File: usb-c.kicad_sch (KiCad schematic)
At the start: 16 parts, among them IC1 USBLC6-2SC6, IC2 632723100011, IC3 TCPP01-M12, Q1 STL11N3LLH6

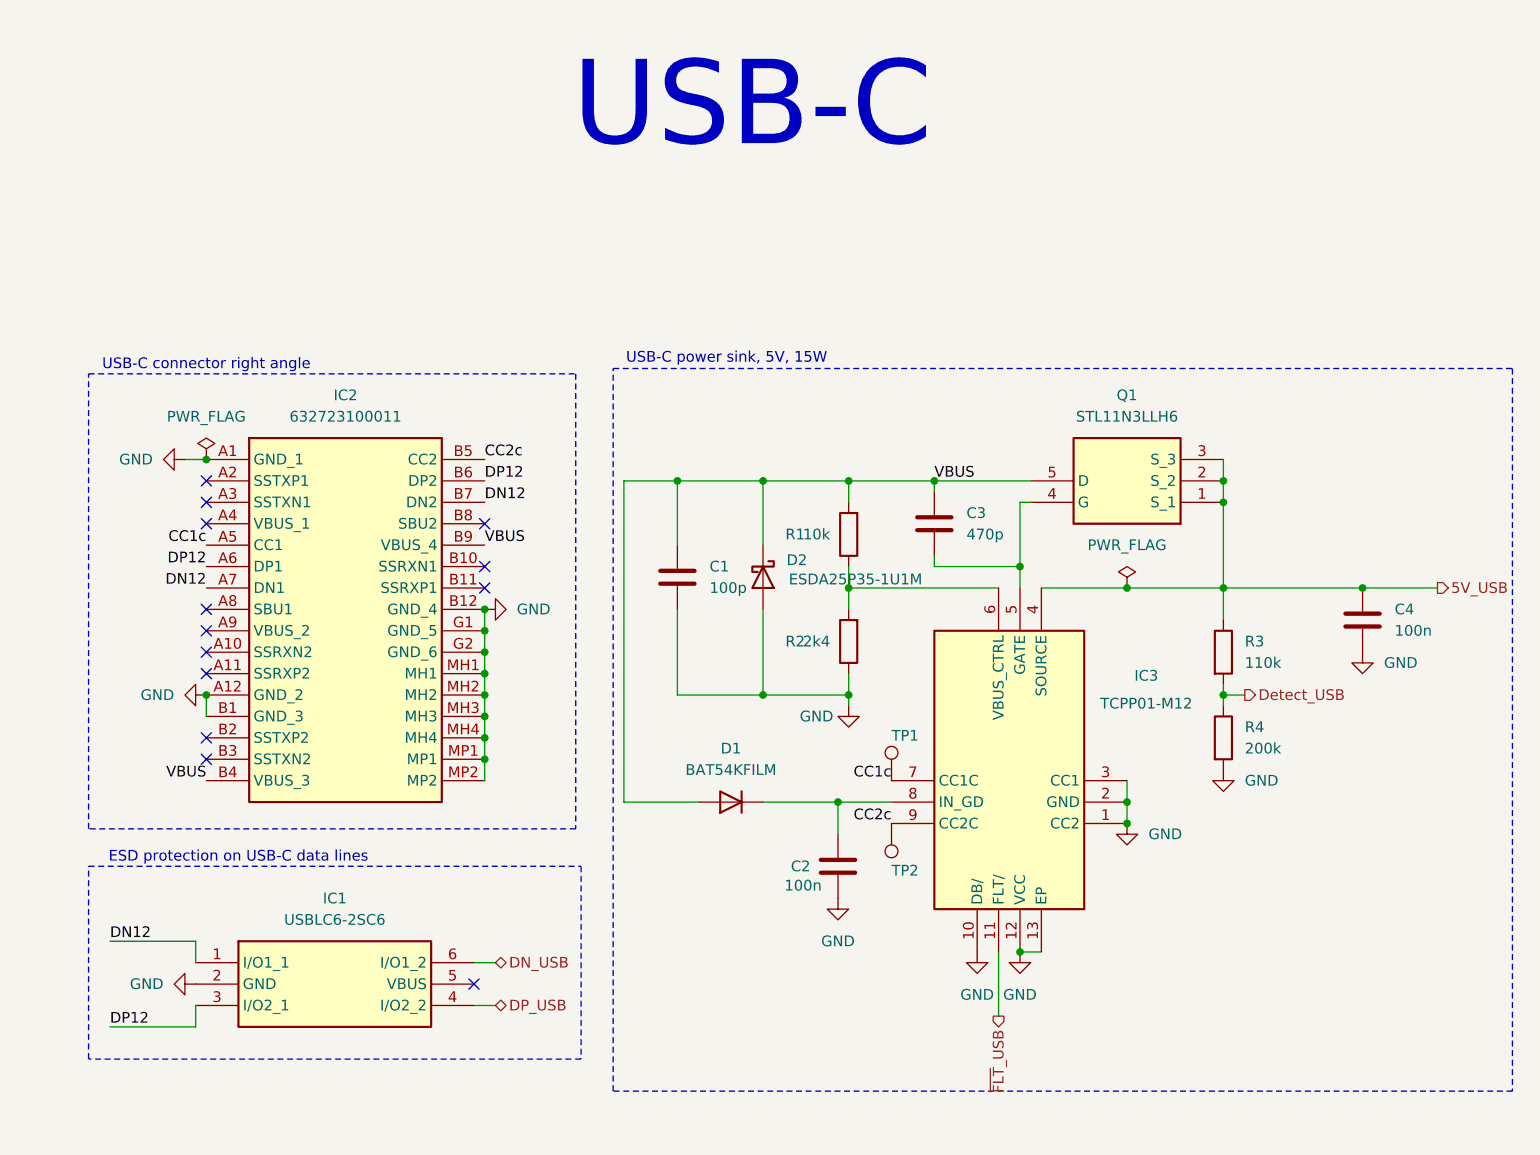
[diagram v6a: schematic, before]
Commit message: Set I2C address for BMP sensors and document address
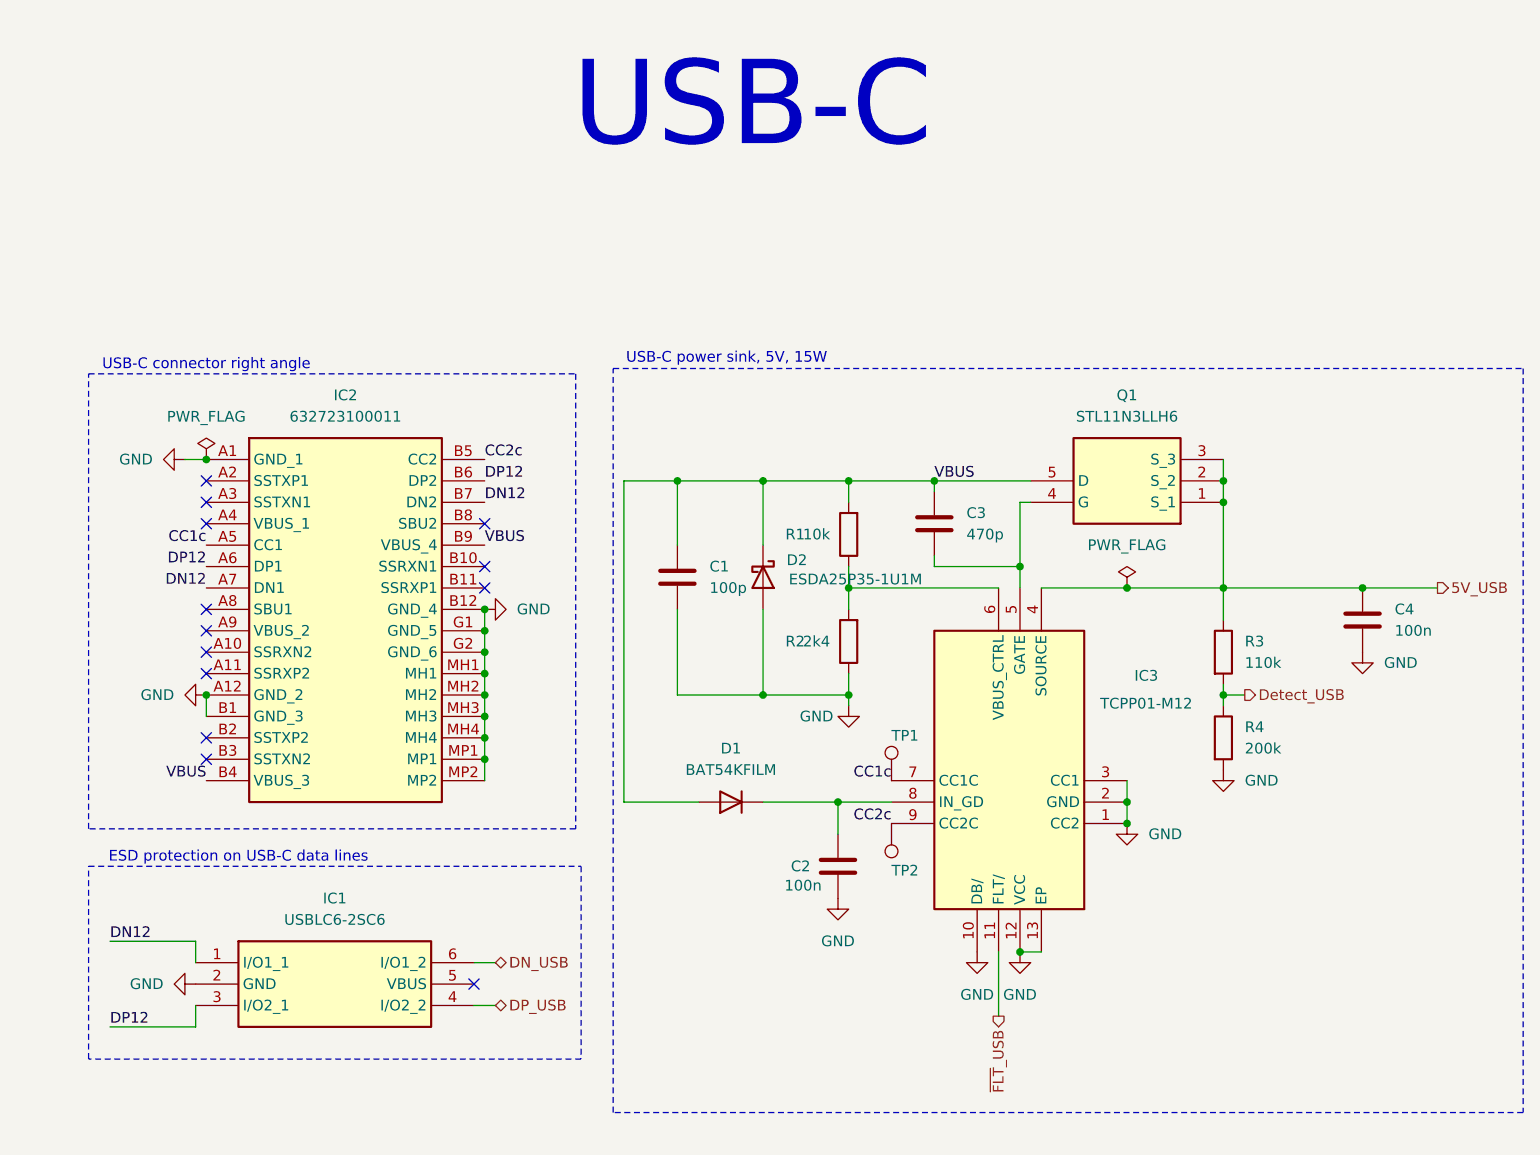
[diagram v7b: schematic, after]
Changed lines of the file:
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@@
 	(rectangle
 		(start 129.54 55.245)
-		(end 236.22 140.97)
+		(end 237.49 143.51)
 		(stroke
 			(width 0)
